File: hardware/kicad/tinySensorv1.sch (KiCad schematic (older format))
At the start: 33 parts, among them J1 RADIO, J10 CR2032 socket, J11 AAA socket, J12 AA Socket, J13 RAW IN, J2 DCDC converter, J3 I2C Sensor (BME/BMP 280), J4 PWM out, J5 OneWire sensor, J6 ISP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

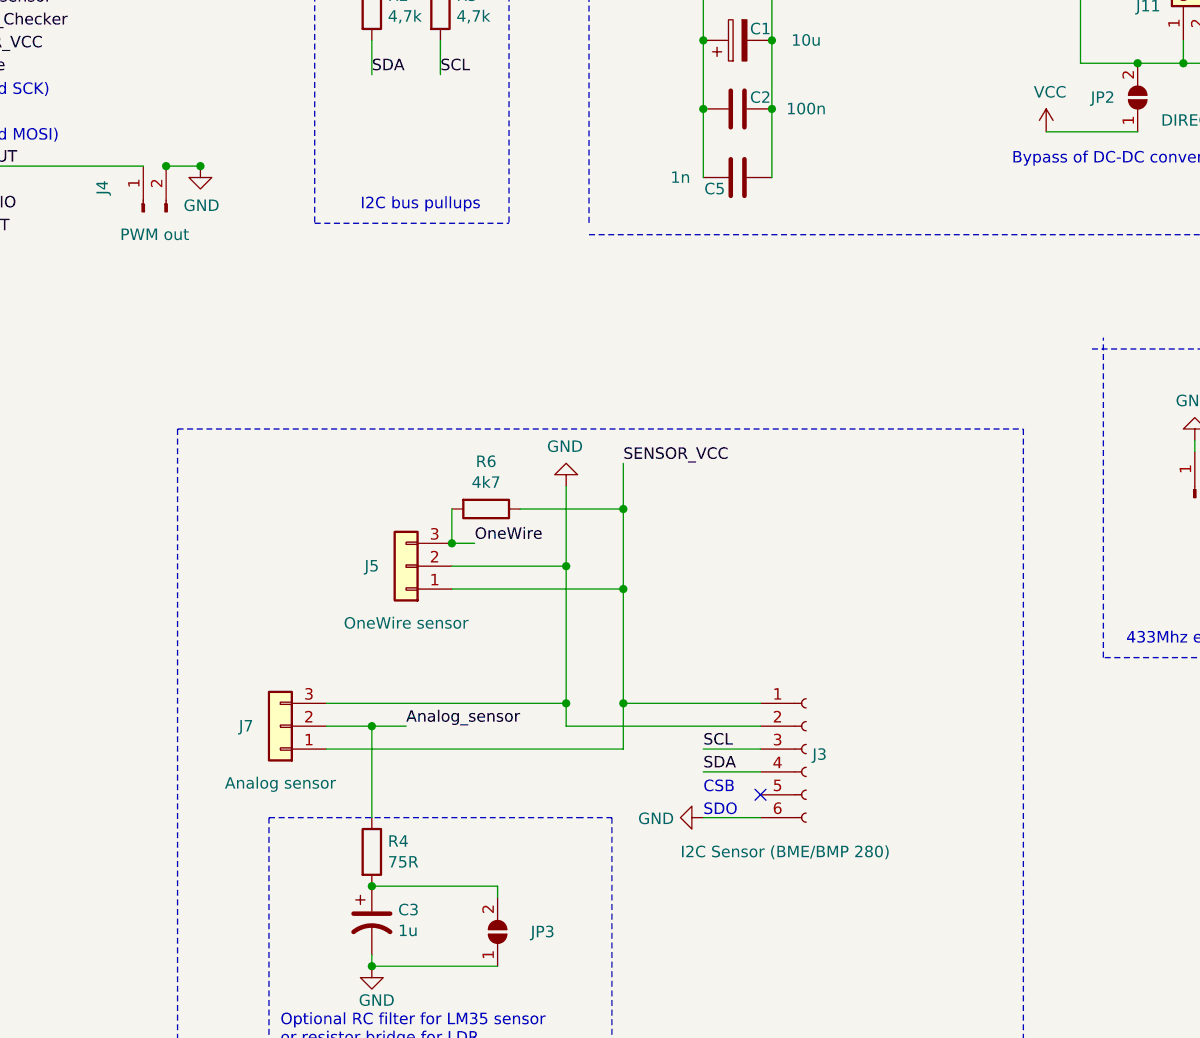
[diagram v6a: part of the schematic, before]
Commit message: feat(board): Allow sub-Vss analog ref for analog sensor
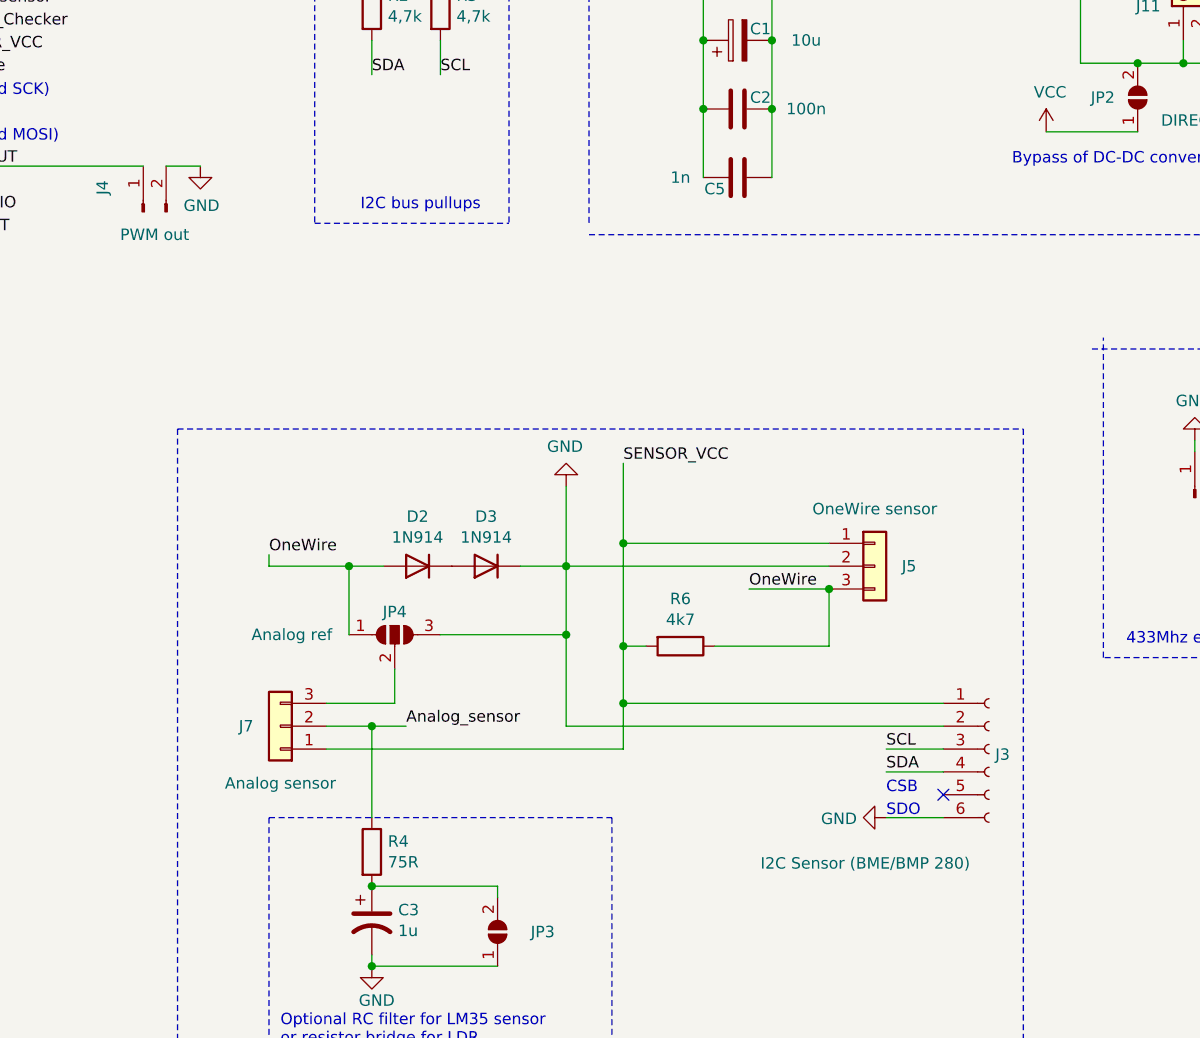
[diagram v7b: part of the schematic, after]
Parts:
- added D2, D3: 1N914, Diode_THT:D_DO-35_SOD27_P7.62mm_Horizontal, symbol Diode:1N914
- added JP4: Analog ref, Jumper:SolderJumper-3_P1.3mm_Open_Pad1.0x1.5mm_NumberLabels, symbol Jumper:SolderJumper_3_Open
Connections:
- net GND: now also D3.1 (K), JP4.3 (B); no longer J7.3 (Pin_3)
- net OneWire: now also R6.1, D2.2 (A), JP4.1 (A); no longer R6.2
- net SENSOR_VCC: now also R6.2; no longer R6.1
- new net: J7.3 (Pin_3), JP4.2 (C)
- new net: D2.1 (K), D3.2 (A)
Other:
- moved on the sheet: J3

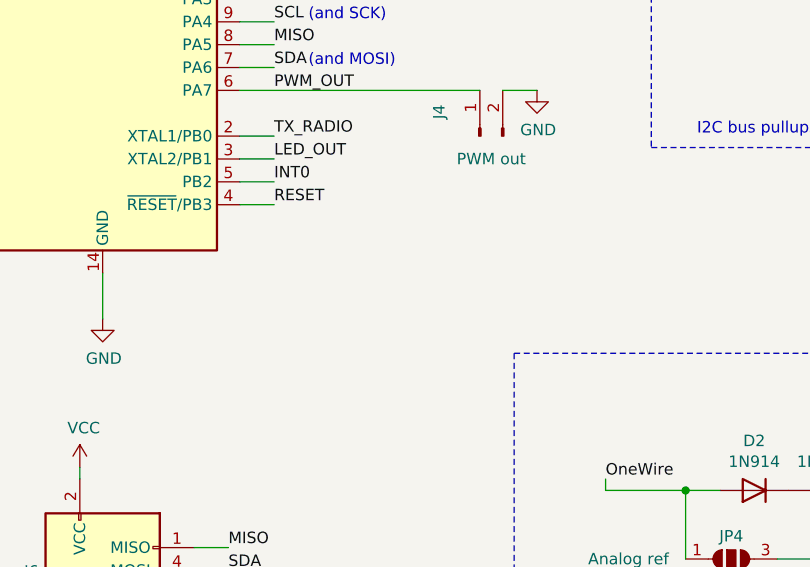
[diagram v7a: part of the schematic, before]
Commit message: Feat: Implement reset button
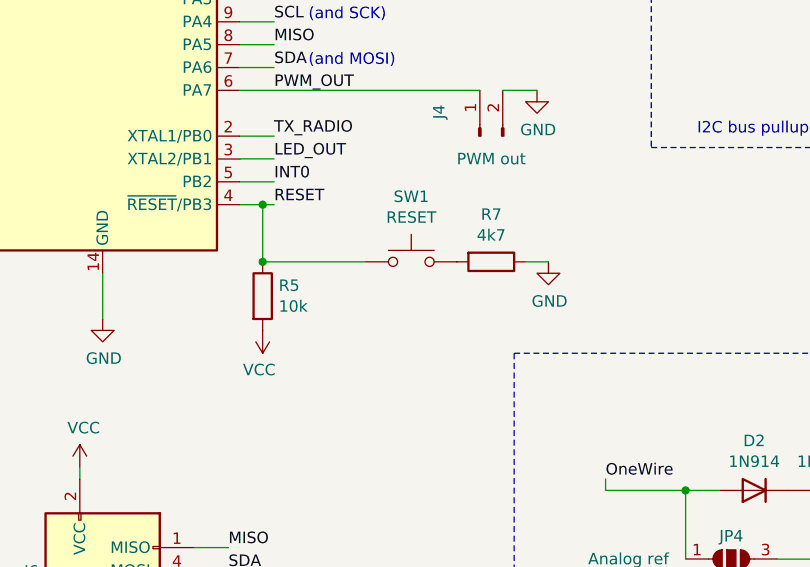
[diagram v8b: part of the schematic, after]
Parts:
- added R5: 10k, Resistor_THT:R_Axial_DIN0204_L3.6mm_D1.6mm_P7.62mm_Horizontal, symbol Device:R
- added R7: 4k7, Resistor_THT:R_Axial_DIN0204_L3.6mm_D1.6mm_P7.62mm_Horizontal, symbol Device:R
- added SW1: RESET, Button_Switch_THT:SW_PUSH_6mm_H4.3mm, symbol Switch:SW_Push
- J12: footprint Battery:BatteryHolder_MPD_BH-18650-PC2 -> Battery:BatteryHolder_Keystone_2460_1xAA
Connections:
- net GND: now also R7.1
- net RESET: now also R5.1, SW1.1
- net VCC: now also R5.2
- new net: R7.2, SW1.2
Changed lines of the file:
@@
 F 0 "J12" V 10250 1450 50  0000 L CNN
 F 1 "AA Socket" V 10450 1200 50  0000 L CNN
-F 2 "Battery:BatteryHolder_MPD_BH-18650-PC2" H 10300 1350 50  0001 C CNN
+F 2 "Battery:BatteryHolder_Keystone_2460_1xAA" H 10300 1350 50  0001 C CNN
 F 3 "~" H 10300 1350 50  0001 C CNN
 	1    10300 1350
@@
 Text Label 3000 2600 0    50   ~ 0
 RESET
-Wire Wire Line
-	2850 2600 3000 2600
 $Comp
 L tinySensorv1-rescue:AVR-ISP-6-Connector J6
@@
 Wire Wire Line
 	4700 4450 5000 4450
+$Comp
+L Device:R R5
+U 1 1 5F9E21D2
+P 2950 3000
+F 0 "R5" H 3020 3046 50  0000 L CNN
+F 1 "10k" H 3020 2955 50  0000 L CNN
+F 2 "Resistor_THT:R_Axial_DIN0204_L3.6mm_D1.6mm_P7.62mm_Horizontal" V 2880 3000 50  0001 C CNN
+F 3 "~" H 2950 3000 50  0001 C CNN
+	1    2950 3000
+	1    0    0    -1
+$EndComp
+$Comp
+L power:VCC #PWR0107
+U 1 1 5F9EC85E
+P 2950 3150
+F 0 "#PWR0107" H 2950 3000 50  0001 C CNN
+F 1 "VCC" H 2965 3323 50  0000 C CNN
+F 2 "" H 2950 3150 50  0001 C CNN
+F 3 "" H 2950 3150 50  0001 C CNN
+	1    2950 3150
+	-1   0    0    1
+$EndComp
+$Comp
+L power:GND #PWR0108
+U 1 1 5F9F6BF3
+P 4200 2850
+F 0 "#PWR0108" H 4200 2600 50  0001 C CNN
+F 1 "GND" H 4205 2677 50  0000 C CNN
+F 2 "" H 4200 2850 50  0001 C CNN
+F 3 "" H 4200 2850 50  0001 C CNN
+	1    4200 2850
+	1    0    0    -1
+$EndComp
+$Comp
+L Device:R R7
+U 1 1 5F9F863D
+P 3950 2850
+F 0 "R7" V 3743 2850 50  0000 C CNN
+F 1 "4k7" V 3834 2850 50  0000 C CNN
+F 2 "Resistor_THT:R_Axial_DIN0204_L3.6mm_D1.6mm_P7.62mm_Horizontal" V 3880 2850 50  0001 C CNN
+F 3 "~" H 3950 2850 50  0001 C CNN
+	1    3950 2850
+	0    1    1    0
+$EndComp
+Wire Wire Line
+	3400 2850 2950 2850
+Wire Wire Line
+	2850 2600 2950 2600
+Wire Wire Line
+	2950 2600 2950 2850
+Connection ~ 2950 2600
+Wire Wire Line
+	2950 2600 3000 2600
+Connection ~ 2950 2850
+Wire Wire Line
+	4200 2850 4100 2850
+$Comp
+L Switch:SW_Push SW1
+U 1 1 5F9F6584
+P 3600 2850
+F 0 "SW1" H 3600 3135 50  0000 C CNN
+F 1 "RESET" H 3600 3044 50  0000 C CNN
+F 2 "Button_Switch_THT:SW_PUSH_6mm_H4.3mm" H 3600 3050 50  0001 C CNN
+F 3 "~" H 3600 3050 50  0001 C CNN
+	1    3600 2850
+	1    0    0    -1
+$EndComp
 $EndSCHEMATC
